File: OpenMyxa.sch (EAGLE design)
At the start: 106 parts, among them CON1 USB, CON2 PINHEAD_1X01-2, CON3 CON-4P-STRAIGHT, CON4 CON-4P-STRAIGHT, CON5 CON-4P-STRAIGHT, CON6 CON-4P-STRAIGHT, CON7 CON-4P-STRAIGHT, CON8 CON-6P, CON9 PINHEAD_1X01-2, IC1 TPD3S014DBVR-SOT23-6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

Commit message: V0.2 import
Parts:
- removed D3: TPSMC62A, TVS_diodes:TPSMC62A
- removed MODULE1: MITOHONDRIQUE, mitohondrique:MITOHONDRIQUE
- added MODULE2: MITOHONDRIQUE-TH, zubax_modules:MITOHONDRIQUE-TH
- CON3, CON4, CON5, CON6: device myxa_masterlib:CON-4P-STRAIGHT -> Connectors:CON-4P-STRAIGHT
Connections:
- removed net N$23: CON3.2, CON4.2, IC3.CANL
- removed net N$24: CON7.2, R25.2
- removed net N$35: CON3.3, CON4.3, IC3.CANH
- new net LED_BLUE: MODULE2.RGB_LED_B, R11.2
- new net N$21: CON3.2, CON4.2, IC3.CANH
- new net N$22: CON3.3, CON4.3, IC3.CANL
- net BEC_ENABLE_OUT: now also MODULE2.BEC_ENABLE_OUT; no longer MODULE1.BEC_ENABLE_OUT
- net CAN1_LED: now also MODULE2.CAN1_LED; no longer MODULE1.CAN1_LED
- net CAN1_RX: now also MODULE2.CAN1_RX; no longer MODULE1.CAN1_RX
- net CAN1_TX: now also MODULE2.CAN1_TX; no longer MODULE1.CAN1_TX
- net CAN1_VDD: now also CON3.1, CON4.1; no longer CON3.4, CON4.4
- net CAN2_LED: now also MODULE2.CAN2_LED; no longer MODULE1.CAN2_LED
- net CAN2_RX: now also MODULE2.CAN2_RX; no longer MODULE1.CAN2_RX
- net CAN2_TX: now also MODULE2.CAN2_TX; no longer MODULE1.CAN2_TX
- net CAN2_VDD: now also CON5.1, CON6.1; no longer CON5.4, CON6.4
- net GAIN_OUT: now also MODULE2.GAIN_OUT; no longer MODULE1.GAIN_OUT
- net GATE_ENABLE_OUT: now also MODULE2.GATE_ENABLE_OUT; no longer MODULE1.GATE_ENABLE_OUT
- net GND: now also CON7.4, MODULE2.GND; no longer CON7.1, MODULE1.GND
- net GNDD: now also CON3.4, CON4.4, CON5.4, CON6.4; no longer CON3.1, CON4.1, CON5.1, CON6.1
- net GPIO1: now also MODULE2.GPIO2; no longer MODULE1.GPIO2
- net GPIO2: now also MODULE2.GPIO1; no longer MODULE1.GPIO1
- net LED_GREEN: now also MODULE2.RGB_LED_G; no longer MODULE1.RGB_LED_G
- net LED_RED: now also MODULE2.RGB_LED_R; no longer MODULE1.RGB_LED_R
- net N$18: now also MODULE2.OVERCURRENT_PROTECT_ADJ; no longer MODULE1.OVERCURRENT_PROTECT_ADJ
- net N$19: now also CON7.2, R8.2; no longer CON7.4, F1.1
- net N$20: now also R25.2; no longer R8.2
- net N$44: now also CON5.3, CON6.3; no longer CON5.2, CON6.2
- net N$46: now also CON5.2, CON6.2; no longer CON5.3, CON6.3
- net N$5: now also MODULE2.USB_VBUS; no longer MODULE1.USB_VBUS
- net N$51: now also MODULE2.USB-; no longer MODULE1.USB-
- net N$55: now also MODULE2.USB+; no longer MODULE1.USB+
- net N$6: now also CON7.1, F1.1; no longer MODULE1.RGB_LED_B, R11.2
- net PGND: no longer D3.A
- net PHASE_A: now also MODULE2.PHASE_A; no longer MODULE1.PHASE_A
- net PHASE_A_CURRENT_SHUNT_N: now also MODULE2.PHASE_A_CURRENT_SHUNT_N; no longer MODULE1.PHASE_A_CURRENT_SHUNT_N
- net PHASE_A_CURRENT_SHUNT_P: now also MODULE2.PHASE_A_CURRENT_SHUNT_P; no longer MODULE1.PHASE_A_CURRENT_SHUNT_P
- net PHASE_A_GATE_HIGH: now also MODULE2.PHASE_A_GATE_HIGH; no longer MODULE1.PHASE_A_GATE_HIGH
- net PHASE_A_GATE_LOW: now also MODULE2.PHASE_A_GATE_LOW; no longer MODULE1.PHASE_A_GATE_LOW
- net PHASE_A_GND: now also MODULE2.PHASE_A_GND; no longer MODULE1.PHASE_A_GND
- net PHASE_B: now also MODULE2.PHASE_B; no longer MODULE1.PHASE_B
- net PHASE_B_CURRENT_SHUNT_N: now also MODULE2.PHASE_B_CURRENT_SHUNT_N; no longer MODULE1.PHASE_B_CURRENT_SHUNT_N
- net PHASE_B_CURRENT_SHUNT_P: now also MODULE2.PHASE_B_CURRENT_SHUNT_P; no longer MODULE1.PHASE_B_CURRENT_SHUNT_P
- net PHASE_B_GATE_HIGH: now also MODULE2.PHASE_B_GATE_HIGH; no longer MODULE1.PHASE_B_GATE_HIGH
- net PHASE_B_GATE_LOW: now also MODULE2.PHASE_B_GATE_LOW; no longer MODULE1.PHASE_B_GATE_LOW
- net PHASE_B_GND: now also MODULE2.PHASE_B_GND; no longer MODULE1.PHASE_B_GND
- net PHASE_C: now also MODULE2.PHASE_C; no longer MODULE1.PHASE_C
- net PHASE_C_GATE_HIGH: now also MODULE2.PHASE_C_GATE_HIGH; no longer MODULE1.PHASE_C_GATE_HIGH
- net PHASE_C_GATE_LOW: now also MODULE2.PHASE_C_GATE_LOW; no longer MODULE1.PHASE_C_GATE_LOW
- net PHASE_C_GND: now also MODULE2.PHASE_C_GND; no longer MODULE1.PHASE_C_GND
- net TEMPERATURE_SENSOR: now also MODULE2.TEMPERATURE_SENSOR; no longer MODULE1.TEMPERATURE_SENSOR
- net UART_RX: now also MODULE2.UART_RX, R29.2; no longer MODULE1.UART_RX, R28.2
- net UART_TX: now also MODULE2.UART_TX, R28.2; no longer MODULE1.UART_TX, R29.2
- net VDC: now also MODULE2.VDC; no longer D3.C, MODULE1.VDC
- net VDD_5V: now also MODULE2.5V_OUT; no longer MODULE1.5V_OUT
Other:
- note added: "Current version 0.2"
- note added: "Whats new -Mitochondrik footprint fixed -DCP connector goes to the bottom side of the PCB -DCP UART pinout fixed -One TVS diode is removed from bottom side of the pcb"

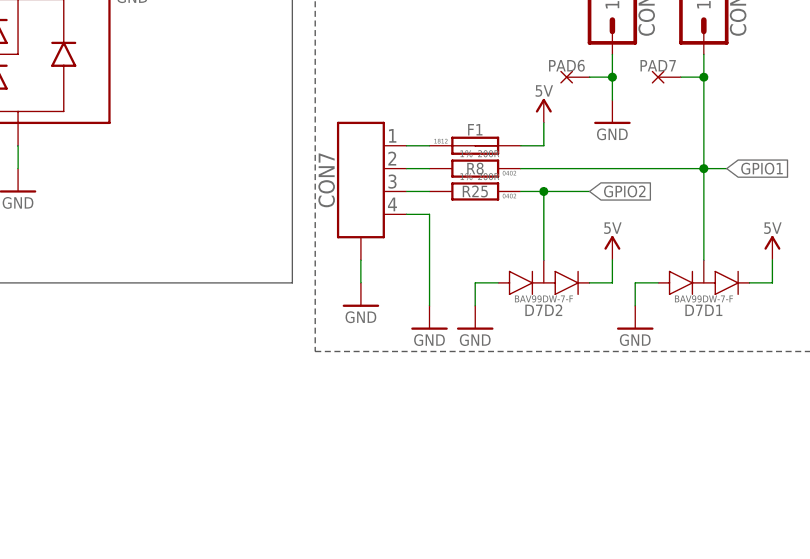
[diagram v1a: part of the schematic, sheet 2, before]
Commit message: Connectors color fix
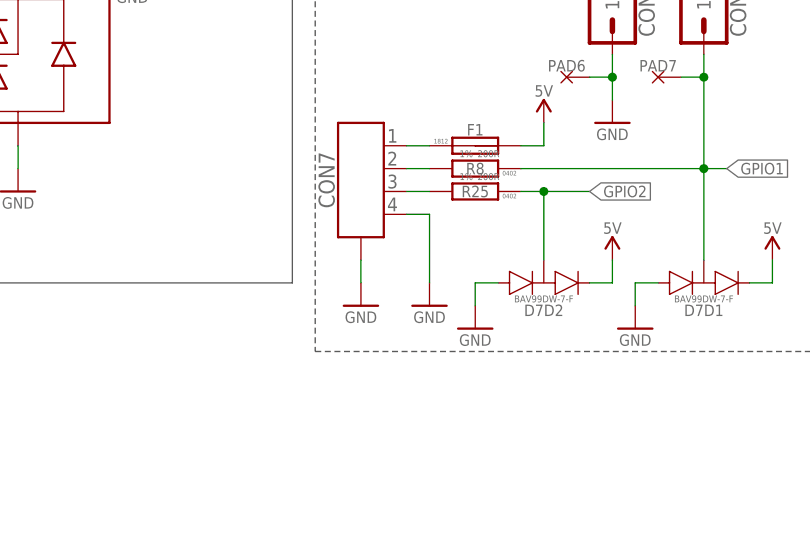
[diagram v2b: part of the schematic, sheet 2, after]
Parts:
- CON3, CON4, CON5, CON6, CON7: value CON-4P-STRAIGHT -> CON-4P-TABS-STRAIGHT; device Connectors:CON-4P-STRAIGHT -> Connectors:CON-4P-TABS-STRAIGHT

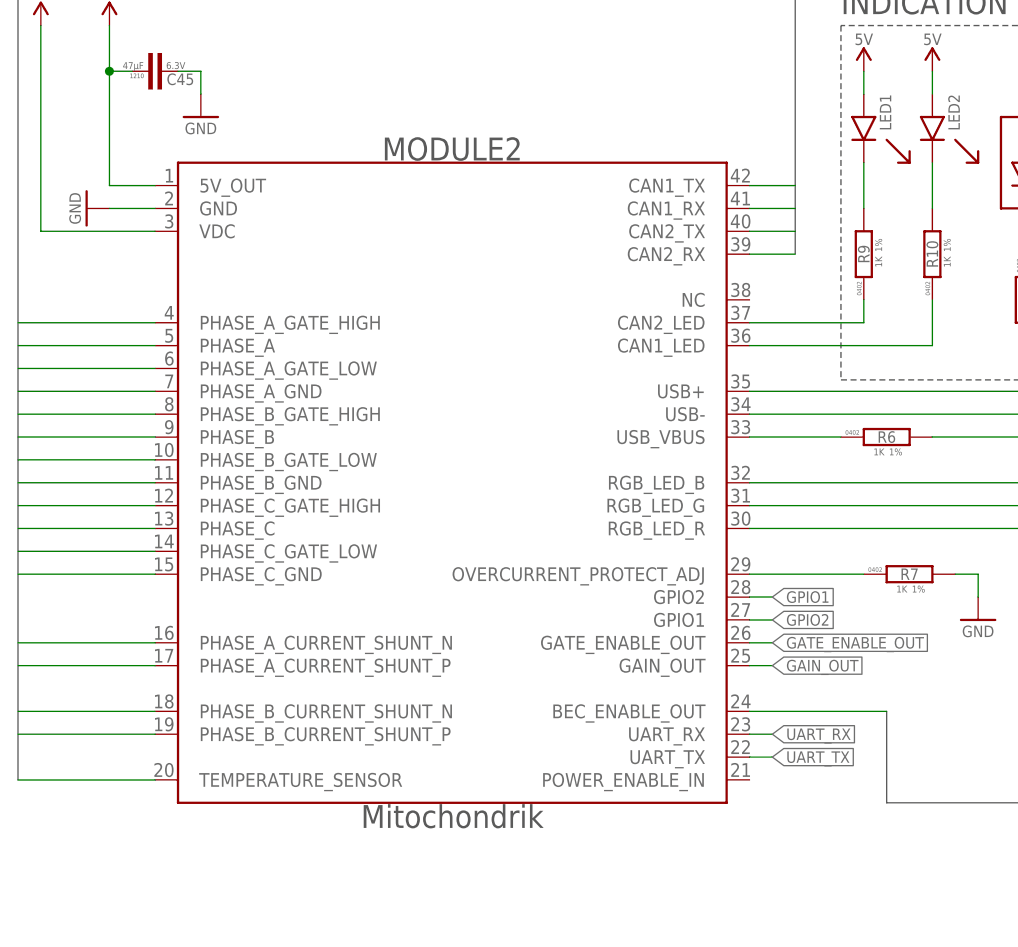
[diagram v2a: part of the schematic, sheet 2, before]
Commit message: Migration to updated mitochondrik library
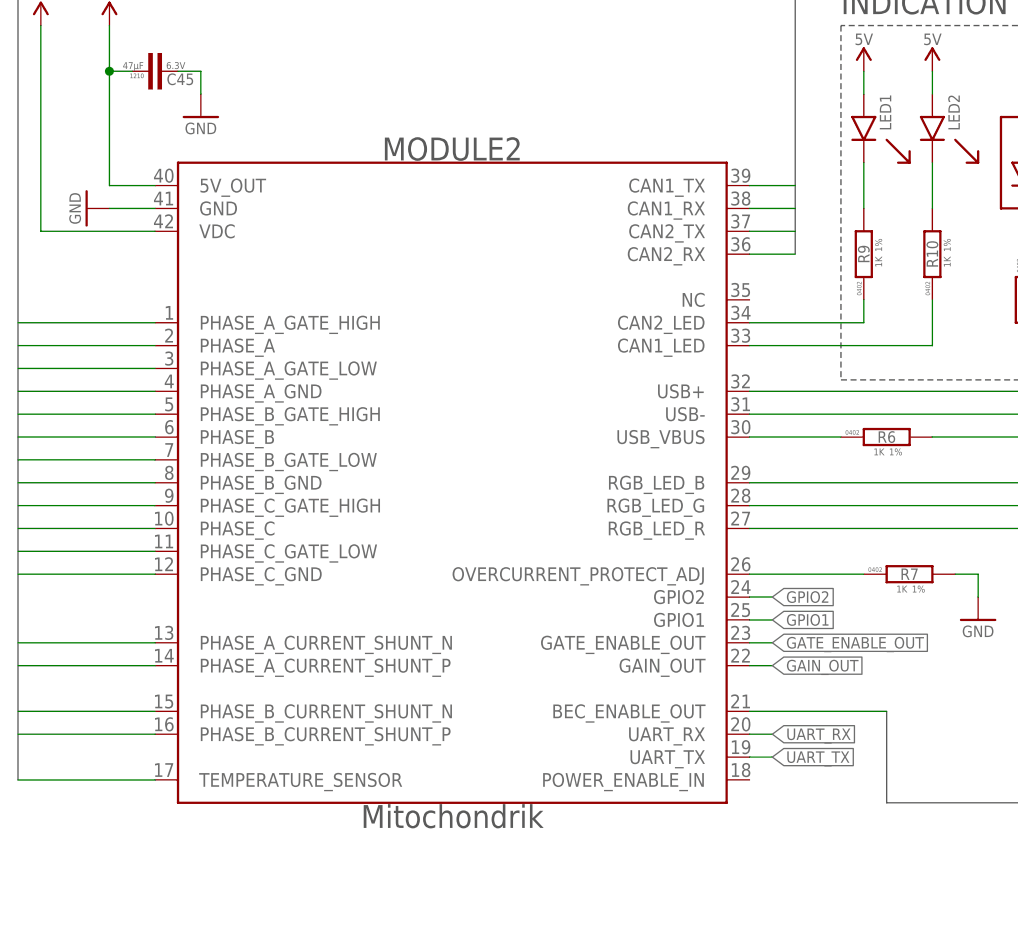
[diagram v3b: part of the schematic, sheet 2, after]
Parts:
- MODULE2: value MITOHONDRIQUE-TH -> MITOHONDRIQUE_V0.2-TH; device zubax_modules:MITOHONDRIQUE-TH -> zubax_modules:MITOHONDRIQUE_V0.2-TH
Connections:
- net GPIO1: now also MODULE2.GPIO1; no longer MODULE2.GPIO2
- net GPIO2: now also MODULE2.GPIO2; no longer MODULE2.GPIO1
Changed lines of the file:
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@@
 <?xml version="1.0" encoding="utf-8"?>
 <!DOCTYPE eagle SYSTEM "eagle.dtd">
-<eagle version="9.3.2">
+<eagle version="9.5.1">
 <drawing>
 <settings>
@@
 <layer number="117" name="bMeasures" color="7" fill="1" visible="no" active="yes"/>
 <layer number="118" name="Rect_Pads" color="7" fill="1" visible="yes" active="yes"/>
+<layer number="119" name="KAP_TEKEN" color="7" fill="1" visible="no" active="no"/>
+<layer number="119" name="KAP_TEKEN" color="7" fill="1" visible="no" active="no"/>
+<layer number="120" name="KAP_MAAT1" color="7" fill="1" visible="no" active="no"/>
+<layer number="120" name="KAP_MAAT1" color="7" fill="1" visible="no" active="no"/>
 <layer number="121" name="_tsilk" color="7" fill="1" visible="yes" active="yes"/>
 <layer number="122" name="_bsilk" color="7" fill="1" visible="yes" active="yes"/>
@@
 <layer number="131" name="tAdjust" color="7" fill="1" visible="yes" active="yes"/>
 <layer number="132" name="bAdjust" color="7" fill="1" visible="yes" active="yes"/>
+<layer number="133" name="bottom_silk" color="7" fill="1" visible="no" active="yes"/>
+<layer number="133" name="bottom_silk" color="7" fill="1" visible="no" active="yes"/>
 <layer number="144" name="Drill_legend" color="7" fill="1" visible="yes" active="yes"/>
 <layer number="145" name="DrillLegend_01-16" color="2" fill="9" visible="yes" active="yes"/>
@@
 <part name="C14" library="C_digikey" library_urn="urn:adsk.eagle:library:2539367" deviceset="4.7µF" device="-0603" package3d_urn="urn:adsk.eagle:package:2539381/2" technology="-25V_10%_X6S" value="4.7µF"/>
 <part name="+P23" library="supply_symbols" library_urn="urn:adsk.eagle:library:5017758" deviceset="5V" device=""/>
-<part name="MODULE2" library="zubax_modules" library_urn="urn:adsk.eagle:library:5014895" deviceset="MITOHONDRIQUE" device="-TH" package3d_urn="urn:adsk.eagle:package:4410646/11"/>
 <part name="FRAME2" library="frames" library_urn="urn:adsk.eagle:library:229" deviceset="A5L-LOC" device=""/>
 <part name="CON3" library="Connectors" library_urn="urn:adsk.eagle:library:3750510" deviceset="CON-4P-TABS" device="-STRAIGHT" package3d_urn="urn:adsk.eagle:package:3587964/5"/>
@@
 <part name="CON6" library="Connectors" library_urn="urn:adsk.eagle:library:3750510" deviceset="CON-4P-TABS" device="-STRAIGHT" package3d_urn="urn:adsk.eagle:package:3587964/5"/>
 <part name="CON7" library="Connectors" library_urn="urn:adsk.eagle:library:3750510" deviceset="CON-4P-TABS" device="-STRAIGHT" package3d_urn="urn:adsk.eagle:package:3587964/5"/>
+<part name="MODULE2" library="zubax_modules" library_urn="urn:adsk.eagle:library:5014895" deviceset="MITOHONDRIQUE_V0.2" device="-TH" package3d_urn="urn:adsk.eagle:package:4410646/13"/>
 </parts>
 <sheets>
@@
 <attribute name="VALUE" x="203.2" y="59.436" size="1.27" layer="96" font="vector" ratio="15" rot="MR0" align="center"/>
 </instance>
+<instance part="CON3" gate="G$1" x="368.3" y="124.46" smashed="yes" rot="R270">
+<attribute name="NAME" x="374.65" y="118.11" size="1.778" layer="95" font="vector" ratio="15" rot="R90" align="center"/>
+</instance>
+<instance part="CON4" gate="G$1" x="368.3" y="101.6" smashed="yes" rot="R270">
+<attribute name="NAME" x="374.65" y="95.25" size="1.778" layer="95" font="vector" ratio="15" rot="R90" align="center"/>
+</instance>
+<instance part="CON5" gate="G$1" x="368.3" y="78.74" smashed="yes" rot="R270">
+<attribute name="NAME" x="374.65" y="72.39" size="1.778" layer="95" font="vector" ratio="15" rot="R90" align="center"/>
+</instance>
+<instance part="CON6" gate="G$1" x="368.3" y="55.88" smashed="yes" rot="R270">
+<attribute name="NAME" x="374.65" y="49.53" size="1.778" layer="95" font="vector" ratio="15" rot="R90" align="center"/>
+</instance>
+<instance part="CON7" gate="G$1" x="185.42" y="55.88" smashed="yes" rot="MR270">
+<attribute name="NAME" x="179.07" y="49.53" size="1.778" layer="95" font="vector" ratio="15" rot="MR90" align="center"/>
+</instance>
 <instance part="MODULE2" gate="G$1" x="25.4" y="38.1" smashed="yes">
 <attribute name="NAME" x="55.88" y="110.744" size="2.54" layer="97" font="vector" ratio="15" align="center"/>
 <attribute name="MANF#" x="55.88" y="36.576" size="2.54" layer="97" font="vector" ratio="15" align="center"/>
-</instance>
-<instance part="CON3" gate="G$1" x="368.3" y="124.46" smashed="yes" rot="R270">
-<attribute name="NAME" x="374.65" y="118.11" size="1.778" layer="95" font="vector" ratio="15" rot="R90" align="center"/>
-</instance>
-<instance part="CON4" gate="G$1" x="368.3" y="101.6" smashed="yes" rot="R270">
-<attribute name="NAME" x="374.65" y="95.25" size="1.778" layer="95" font="vector" ratio="15" rot="R90" align="center"/>
-</instance>
-<instance part="CON5" gate="G$1" x="368.3" y="78.74" smashed="yes" rot="R270">
-<attribute name="NAME" x="374.65" y="72.39" size="1.778" layer="95" font="vector" ratio="15" rot="R90" align="center"/>
-</instance>
-<instance part="CON6" gate="G$1" x="368.3" y="55.88" smashed="yes" rot="R270">
-<attribute name="NAME" x="374.65" y="49.53" size="1.778" layer="95" font="vector" ratio="15" rot="R90" align="center"/>
-</instance>
-<instance part="CON7" gate="G$1" x="185.42" y="55.88" smashed="yes" rot="MR270">
-<attribute name="NAME" x="179.07" y="49.53" size="1.778" layer="95" font="vector" ratio="15" rot="MR90" align="center"/>
 </instance>
 </instances>
@@
 <net name="GPIO2" class="0">
 <segment>
-<wire x1="88.9" y1="58.42" x2="91.44" y2="58.42" width="0.1524" layer="91"/>
-<label x="91.44" y="58.42" size="1.27" layer="95" xref="yes"/>
-<pinref part="MODULE2" gate="G$1" pin="GPIO1"/>
-</segment>
-<segment>
 <pinref part="R25" gate="G$1" pin="1"/>
 <wire x1="200.66" y1="48.26" x2="203.2" y2="48.26" width="0.1524" layer="91"/>
@@
 <label x="208.28" y="48.26" size="1.27" layer="95" xref="yes"/>
 </segment>
-</net>
-<net name="GPIO1" class="0">
 <segment>
 <wire x1="88.9" y1="60.96" x2="91.44" y2="60.96" width="0.1524" layer="91"/>
@@
 <pinref part="MODULE2" gate="G$1" pin="GPIO2"/>
 </segment>
+</net>
+<net name="GPIO1" class="0">
 <segment>
 <pinref part="R8" gate="G$1" pin="1"/>
@@
 <junction x="220.98" y="60.96"/>
 </segment>
-</net>
+<segment>
+<wire x1="88.9" y1="58.42" x2="91.44" y2="58.42" width="0.1524" layer="91"/>
+<label x="91.44" y="58.42" size="1.27" layer="95" xref="yes"/>
+<pinref part="MODULE2" gate="G$1" pin="GPIO1"/>
+</segment>
+</net>
